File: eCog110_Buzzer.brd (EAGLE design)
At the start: 47.5 x 28 mm, 3 parts

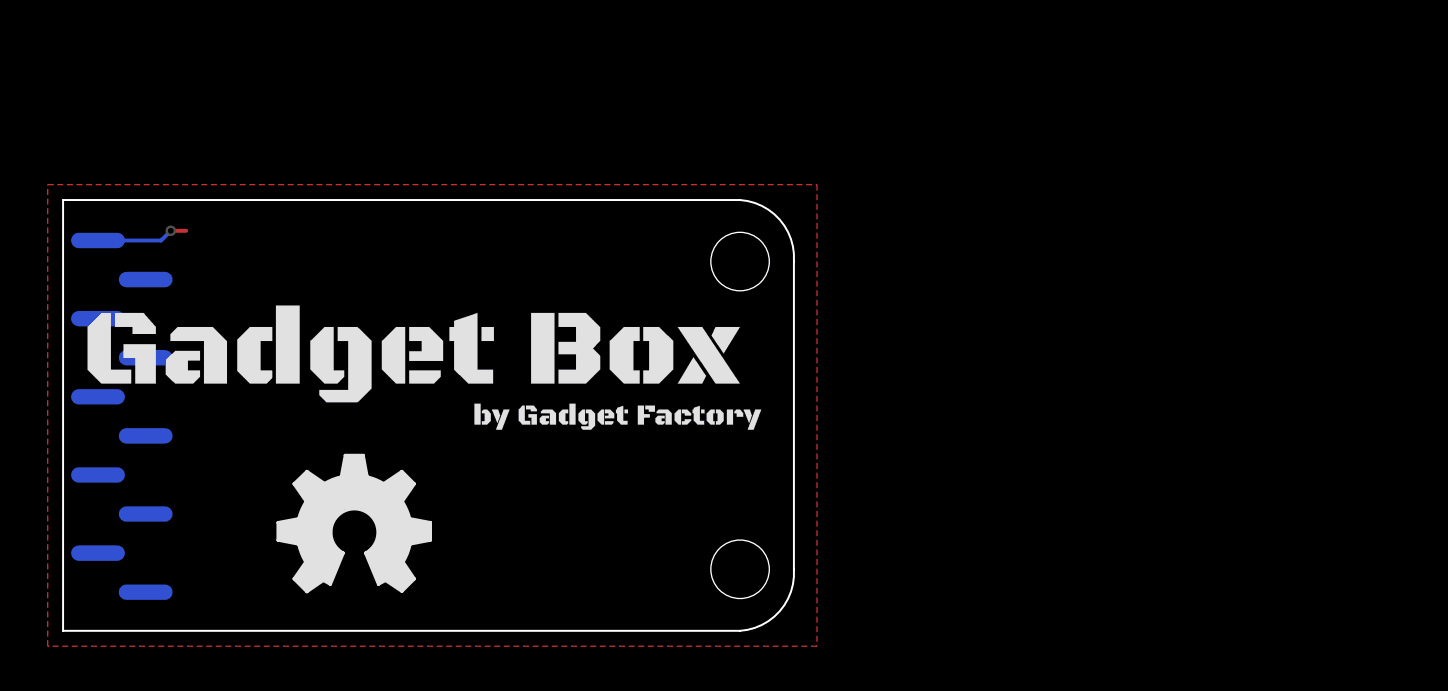
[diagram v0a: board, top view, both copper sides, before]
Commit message: Added new eCogs
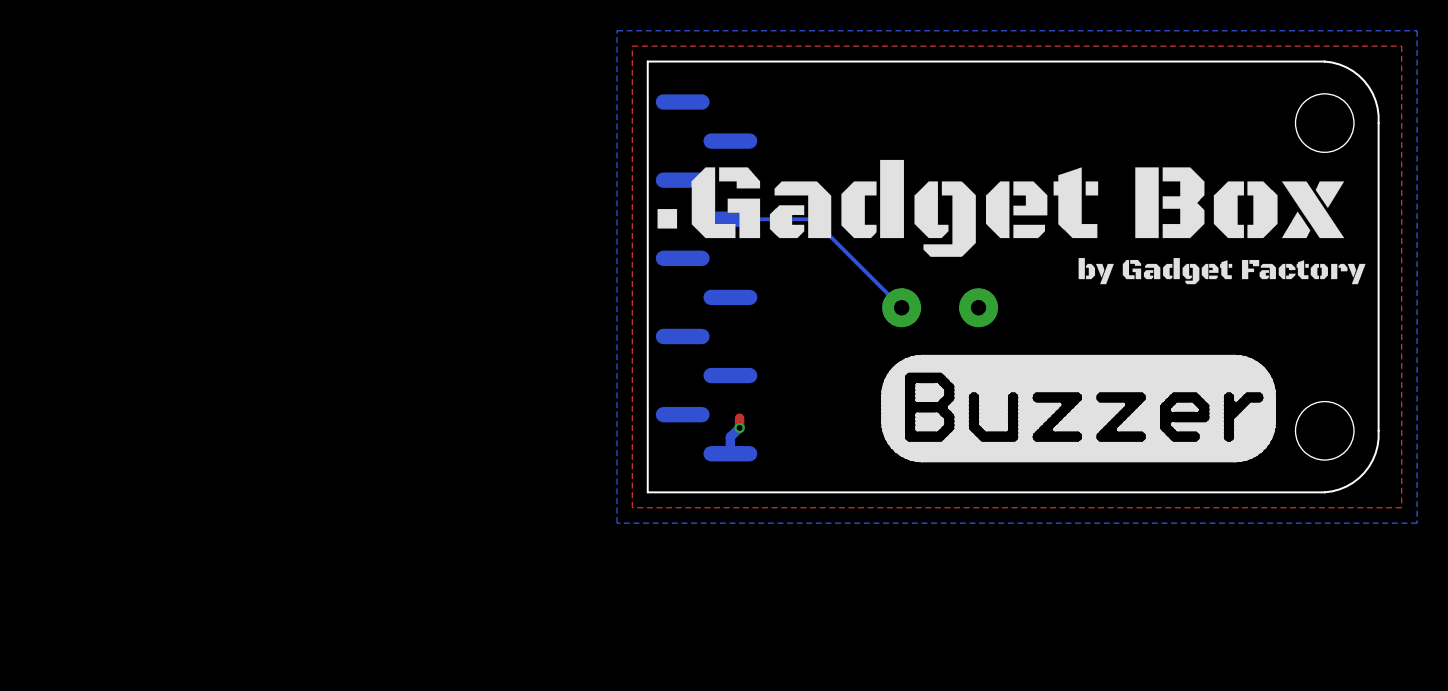
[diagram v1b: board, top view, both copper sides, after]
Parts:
- removed U$2: (no value), GadgetFactory:GADGETBOX_TEXT
- added SP1: SPEAKER/PS12, adafruit:PS12
- added U$4: (no value), eCogs:LEGEND_PWM
- U$1: device ohw-logo:OSHW_FILLX350_NOTEXT -> GadgetFactory:GADGETBOX_TEXT
- moved U$1 54.1 mm to (62.1, 27.2)
- moved ECOG 39.1 mm to (38.0, 9.00)
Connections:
- new net N$1: ECOG.G2, SP1.P$2
- net GND: now also SP1.P$1
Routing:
- net N$1: track 0.00 -> 13.5 mm
- net GND: track 5.99 -> 0.00 mm, vias 1 -> 0
- net 3V3: track 0.00 -> 2.56 mm, vias 0 -> 1
- added copper zone on layer 1, net 3V3
- added copper zone on layer 16, net GND
- removed copper zone on layer 1, net GND
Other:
- board text added: "3.3V"
- board text added: "Buzzer"
- board text added: "GND"
- board text added: "ecog110 v1.0"
- board text added: "ecog110.GadgetFactory.net"
- board text removed: "Blank"
- board text removed: "ecog0 v1.5"
- board text removed: "ecog0.GadgetFactory.net"

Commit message: All the 2.0 updates
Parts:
- moved U$1 39.1 mm to (24.0, 18.4)
- moved ECOG 39.1 mm to (0.00, 0.00)
- moved SP1 36.7 mm to (21.4, 12.1)
- moved U$4 18.3 mm to (47.0, 10.2)
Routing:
- net N$1: track 13.5 -> 9.77 mm
- net 3V3: track 2.56 -> 0.00 mm, vias 1 -> 0
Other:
- outline, holes or cut-outs redrawn
- board text added: "2"
- board text added: "ecog110 v2.0"
- board text removed: "ecog110 v1.0"
